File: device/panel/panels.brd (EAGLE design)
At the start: 133 x 72.5 mm, 0 parts

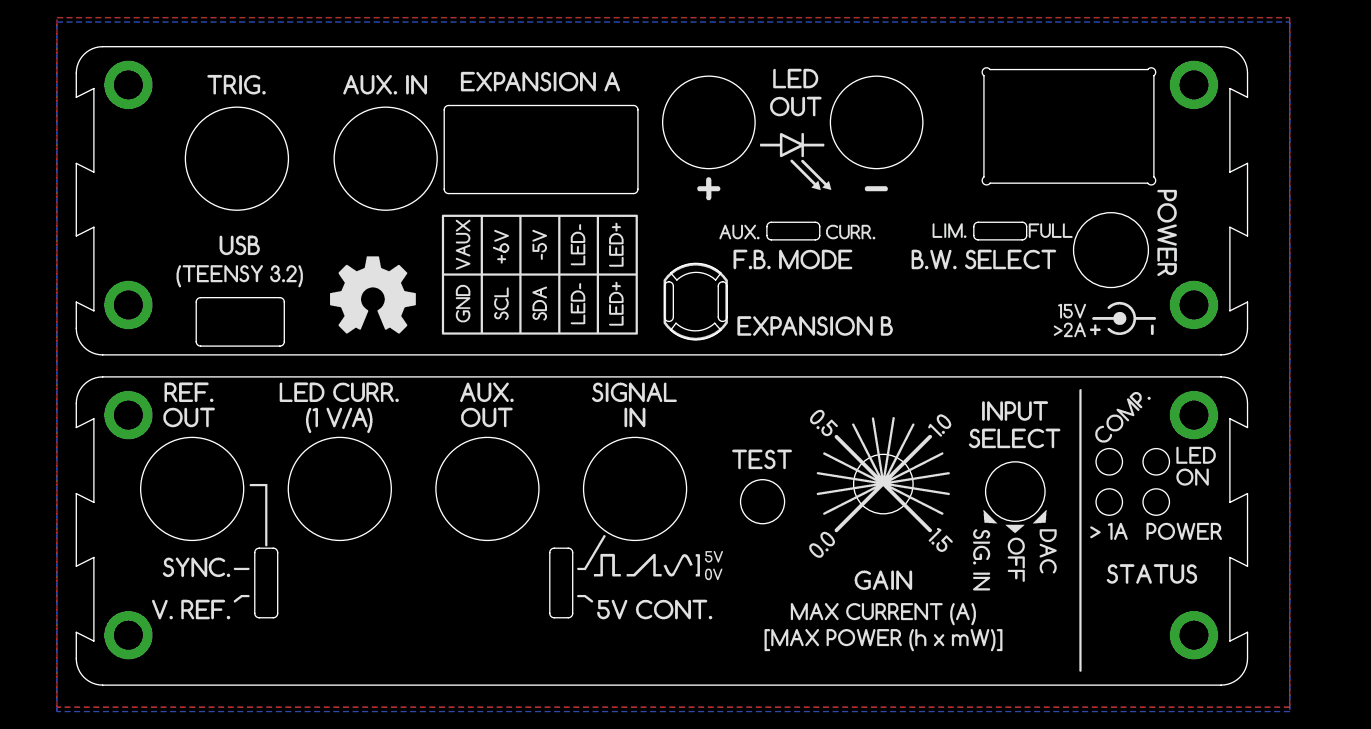
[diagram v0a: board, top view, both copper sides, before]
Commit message: Cyclops 3.7a
- Replace 1 turn pot with 10 turn pot
- Update panels to fit it
- Add JST wire to board connector to connect it
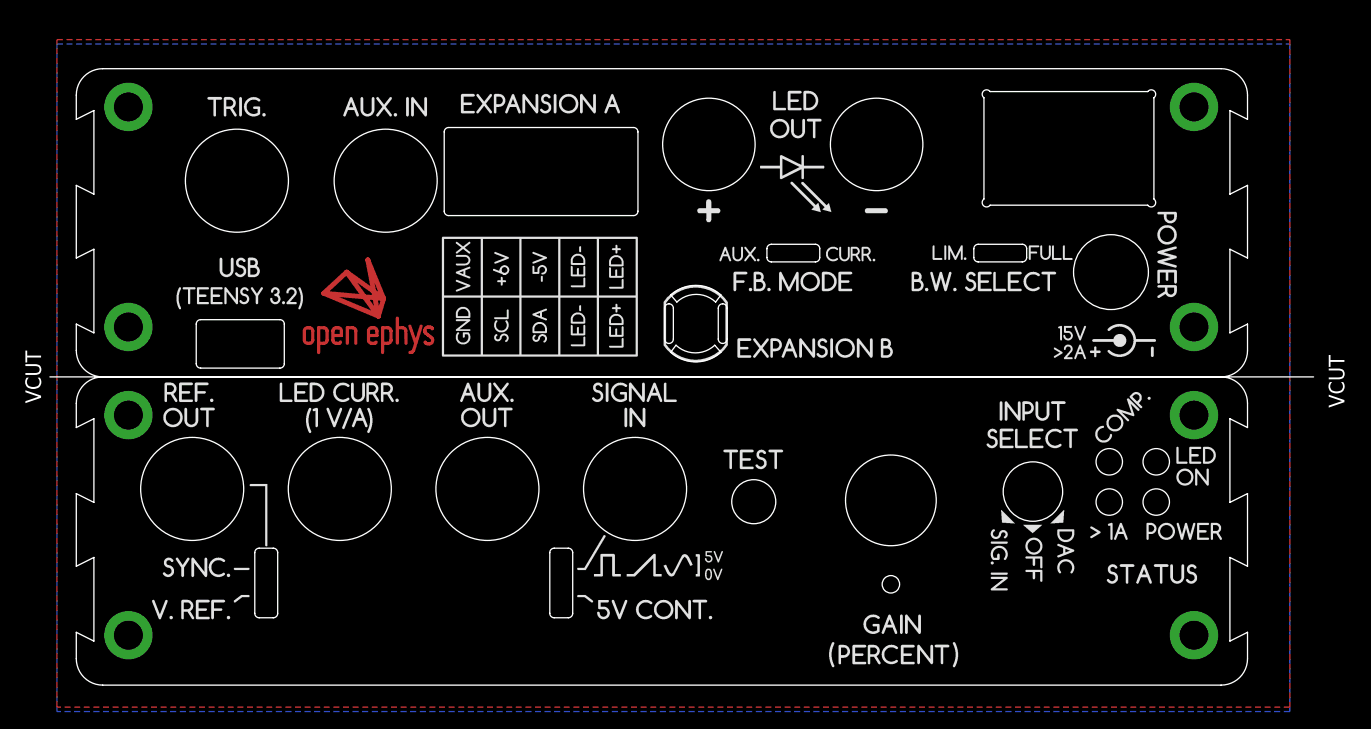
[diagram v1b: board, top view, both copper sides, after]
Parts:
- added E$1: (no value), jonnew:OE-LOGO-14X10
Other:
- board size 133 x 72.5 mm -> 143.5 x 70 mm
- board text added: "VCUT"

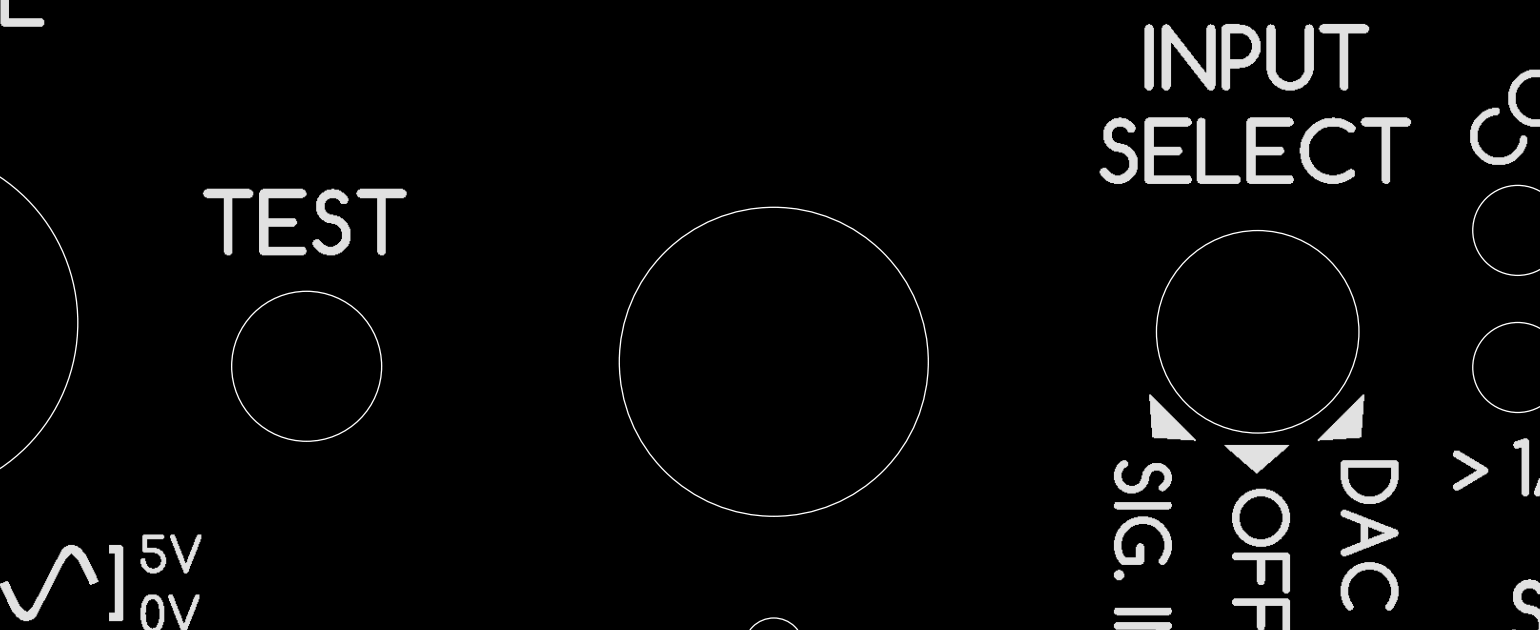
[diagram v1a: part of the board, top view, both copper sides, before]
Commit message: Changes to revision 3.7 after in the field testing
- Some small moves on the panel and pcb for manufacturing purposes
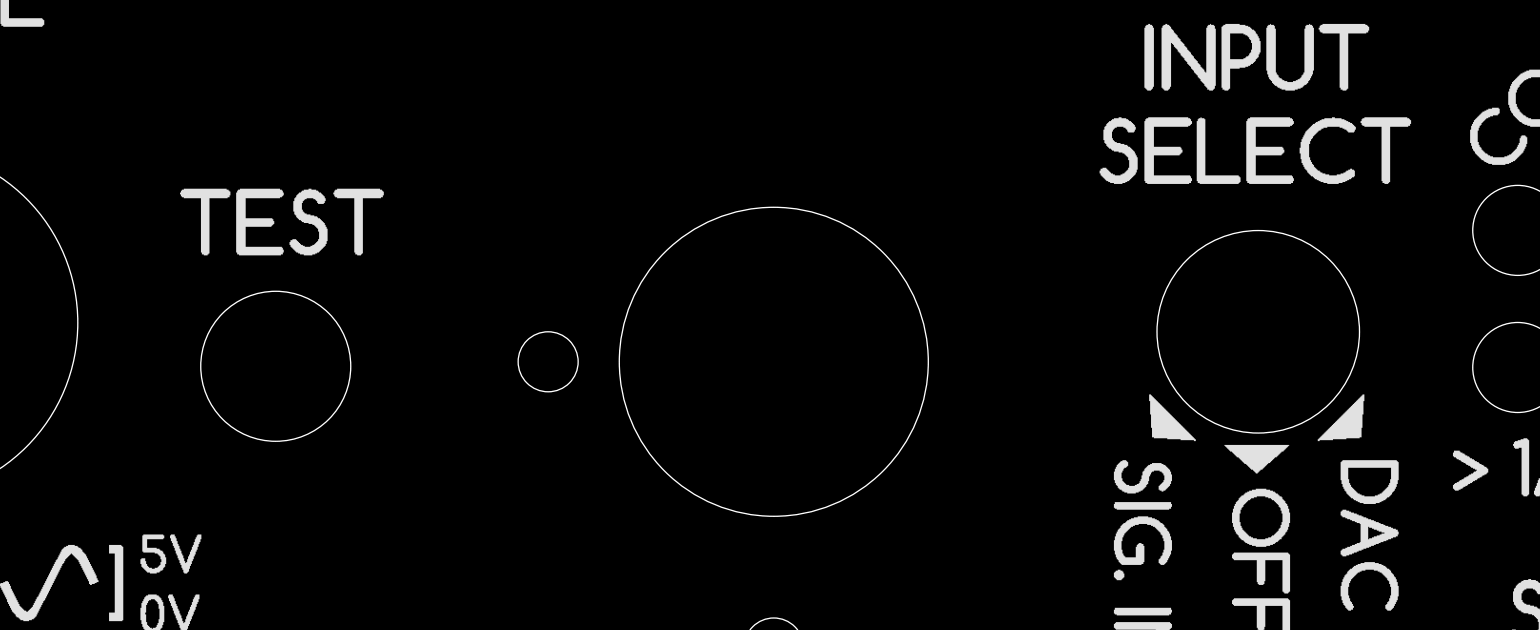
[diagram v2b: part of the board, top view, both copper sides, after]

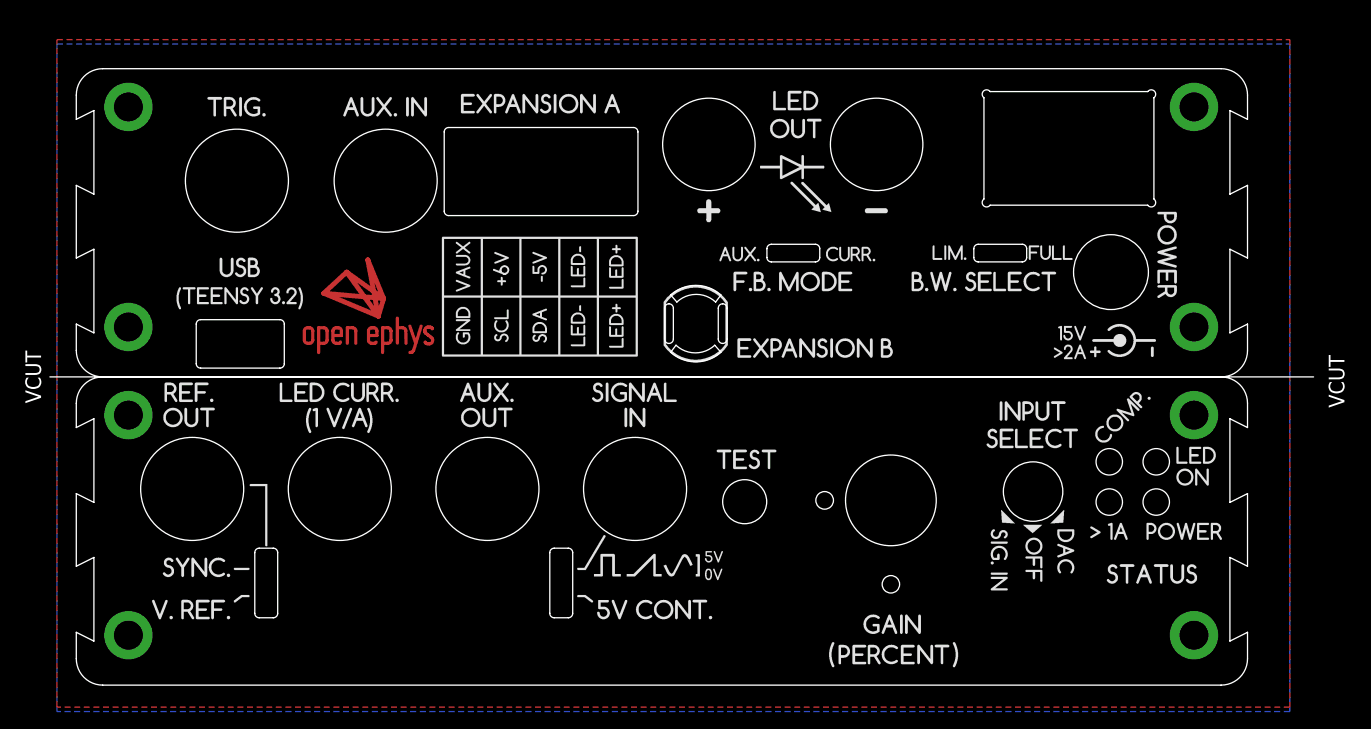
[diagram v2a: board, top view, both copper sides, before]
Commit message: Decreased screws external rings to hide exposed pads below screw heads.
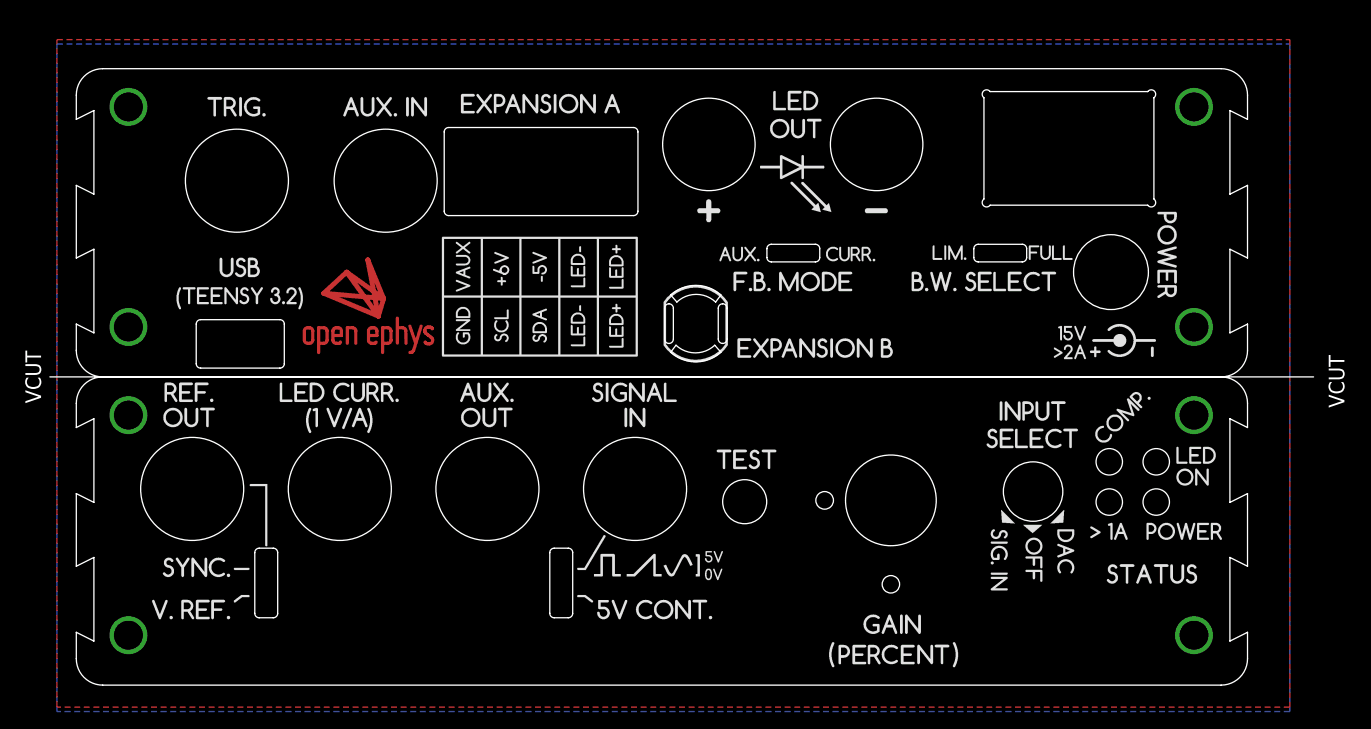
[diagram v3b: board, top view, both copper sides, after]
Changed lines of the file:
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@@
 <?xml version="1.0" encoding="utf-8"?>
 <!DOCTYPE eagle SYSTEM "eagle.dtd">
-<eagle version="8.3.2">
+<eagle version="9.5.1">
 <drawing>
 <settings>
@@
 <setting verticaltext="up"/>
 </settings>
-<grid distance="5" unitdist="mm" unit="mm" style="lines" multiple="1" display="yes" altdistance="0.025" altunitdist="inch" altunit="inch"/>
+<grid distance="0.1" unitdist="mm" unit="mm" style="dots" multiple="1" display="yes" altdistance="0.025" altunitdist="inch" altunit="inch"/>
 <layers>
 <layer number="1" name="Top" color="4" fill="1" visible="yes" active="yes"/>
@@
 <layer number="49" name="Reference" color="7" fill="1" visible="yes" active="yes"/>
 <layer number="50" name="dxf" color="7" fill="1" visible="no" active="no"/>
-<layer number="51" name="tDocu" color="14" fill="1" visible="yes" active="yes"/>
-<layer number="52" name="bDocu" color="7" fill="1" visible="yes" active="yes"/>
+<layer number="51" name="tDocu" color="14" fill="1" visible="no" active="yes"/>
+<layer number="52" name="bDocu" color="7" fill="1" visible="no" active="yes"/>
 <layer number="53" name="tGND_GNDA" color="7" fill="9" visible="no" active="no"/>
 <layer number="54" name="bGND_GNDA" color="1" fill="9" visible="no" active="no"/>
@@
 <param name="dpMaxLengthDifference" value="10mm"/>
 <param name="dpGapFactor" value="2.5"/>
-<param name="checkGrid" value="0"/>
 <param name="checkAngle" value="0"/>
 <param name="checkFont" value="1"/>
 <param name="checkRestrict" value="0"/>
+<param name="checkStop" value="0"/>
+<param name="checkValues" value="0"/>
+<param name="checkNames" value="1"/>
+<param name="checkWireStubs" value="1"/>
+<param name="checkPolygonWidth" value="0"/>
 <param name="useDiameter" value="13"/>
 <param name="maxErrors" value="50"/>
@@
 </autorouter>
 <elements>
-<element name="E$1" library="jonnew" package="OE-LOGO-14X10" value="" x="32.5" y="41.5"/>
+<element name="E$1" library="jonnew" package="OE-LOGO-14X10" value="" x="32.5" y="41.5" smashed="yes"/>
 </elements>
 <signals>
 <signal name="GND">
-<via x="5.921" y="65.66" extent="1-16" drill="3.3" diameter="5.5"/>
+<via x="5.921" y="65.66" extent="1-16" drill="3.3" diameter="4.316"/>
 <polygon width="0.254" layer="16">
 <vertex x="-2.2" y="-3"/>
@@
 <vertex x="137.8" y="-2.5"/>
 </polygon>
-<via x="5.921" y="40.67" extent="1-16" drill="3.3" diameter="5.5"/>
-<via x="126.921" y="40.67" extent="1-16" drill="3.3" diameter="5.5"/>
-<via x="126.921" y="65.66" extent="1-16" drill="3.3" diameter="5.5"/>
-<via x="5.921" y="30.66" extent="1-16" drill="3.3" diameter="5.5"/>
-<via x="5.921" y="5.67" extent="1-16" drill="3.3" diameter="5.5"/>
-<via x="126.921" y="5.67" extent="1-16" drill="3.3" diameter="5.5"/>
-<via x="126.921" y="30.66" extent="1-16" drill="3.3" diameter="5.5"/>
-<wire x1="5.921" y1="40.67" x2="5.921" y2="30.66" width="0" layer="19" extent="1-1"/>
+<via x="5.921" y="40.67" extent="1-16" drill="3.3" diameter="4.316"/>
+<via x="126.921" y="40.67" extent="1-16" drill="3.3" diameter="4.316"/>
+<via x="126.921" y="65.66" extent="1-16" drill="3.3" diameter="4.316"/>
+<via x="5.921" y="30.66" extent="1-16" drill="3.3" diameter="4.316"/>
+<via x="5.921" y="5.67" extent="1-16" drill="3.3" diameter="4.316"/>
+<via x="126.921" y="5.67" extent="1-16" drill="3.3" diameter="4.316"/>
+<via x="126.921" y="30.66" extent="1-16" drill="3.3" diameter="4.316"/>
+<wire x1="126.921" y1="40.67" x2="126.921" y2="65.66" width="0" layer="19" extent="1-1"/>
+<wire x1="126.921" y1="30.66" x2="126.921" y2="40.67" width="0" layer="19" extent="1-1"/>
+<wire x1="126.921" y1="5.67" x2="126.921" y2="30.66" width="0" layer="19" extent="1-1"/>
+<wire x1="5.921" y1="65.66" x2="126.921" y2="65.66" width="0" layer="19" extent="1-1"/>
+<wire x1="5.921" y1="40.67" x2="5.921" y2="65.66" width="0" layer="19" extent="1-1"/>
+<wire x1="5.921" y1="30.66" x2="5.921" y2="40.67" width="0" layer="19" extent="1-1"/>
+<wire x1="5.921" y1="5.67" x2="5.921" y2="30.66" width="0" layer="19" extent="1-1"/>
 </signal>
 </signals>
+<mfgpreviewcolors>
+<mfgpreviewcolor name="soldermaskcolor" color="0xC8008000"/>
+<mfgpreviewcolor name="silkscreencolor" color="0xFFFEFEFE"/>
+<mfgpreviewcolor name="backgroundcolor" color="0xFF282828"/>
+<mfgpreviewcolor name="coppercolor" color="0xFFFFBF00"/>
+<mfgpreviewcolor name="substratecolor" color="0xFF786E46"/>
+</mfgpreviewcolors>
 </board>
 </drawing>
